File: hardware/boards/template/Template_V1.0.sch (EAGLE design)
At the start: 2 parts

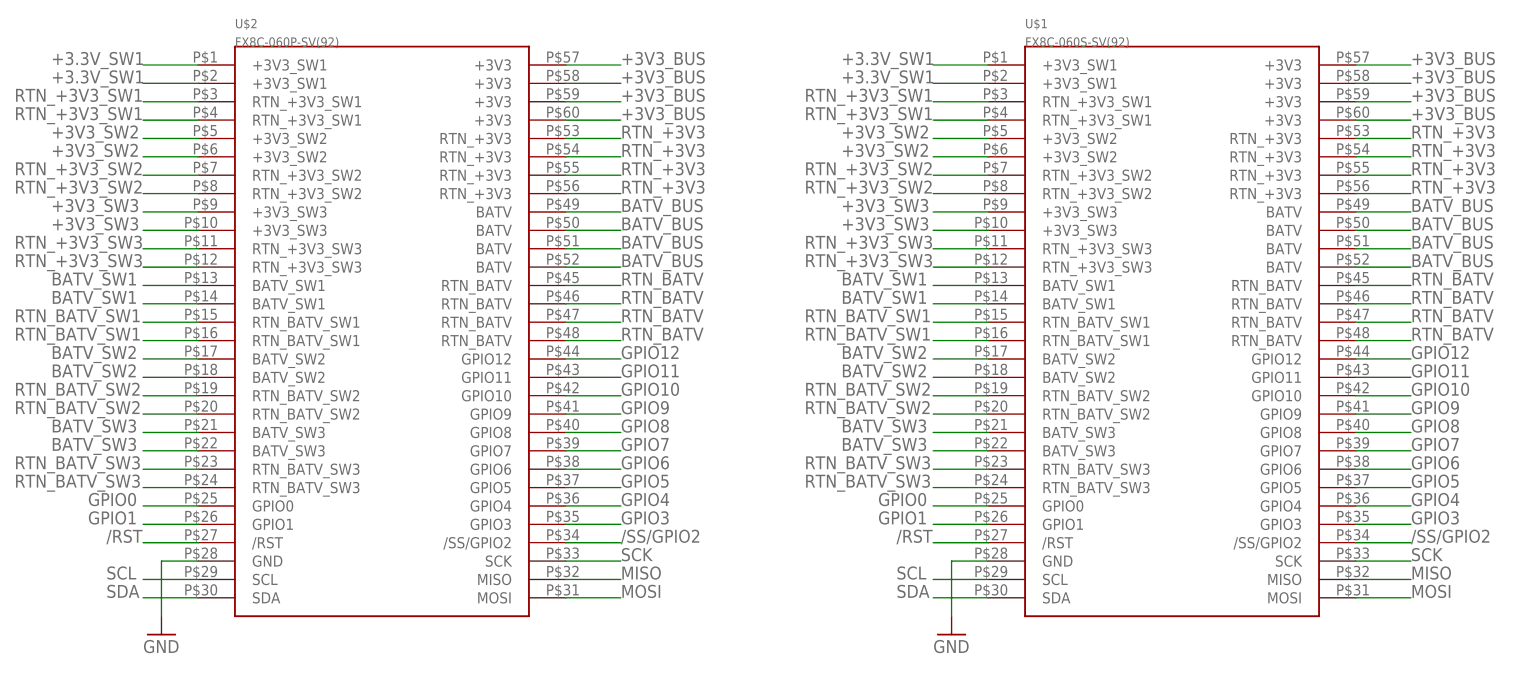
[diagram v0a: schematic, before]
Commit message: fixed fx8c symbols
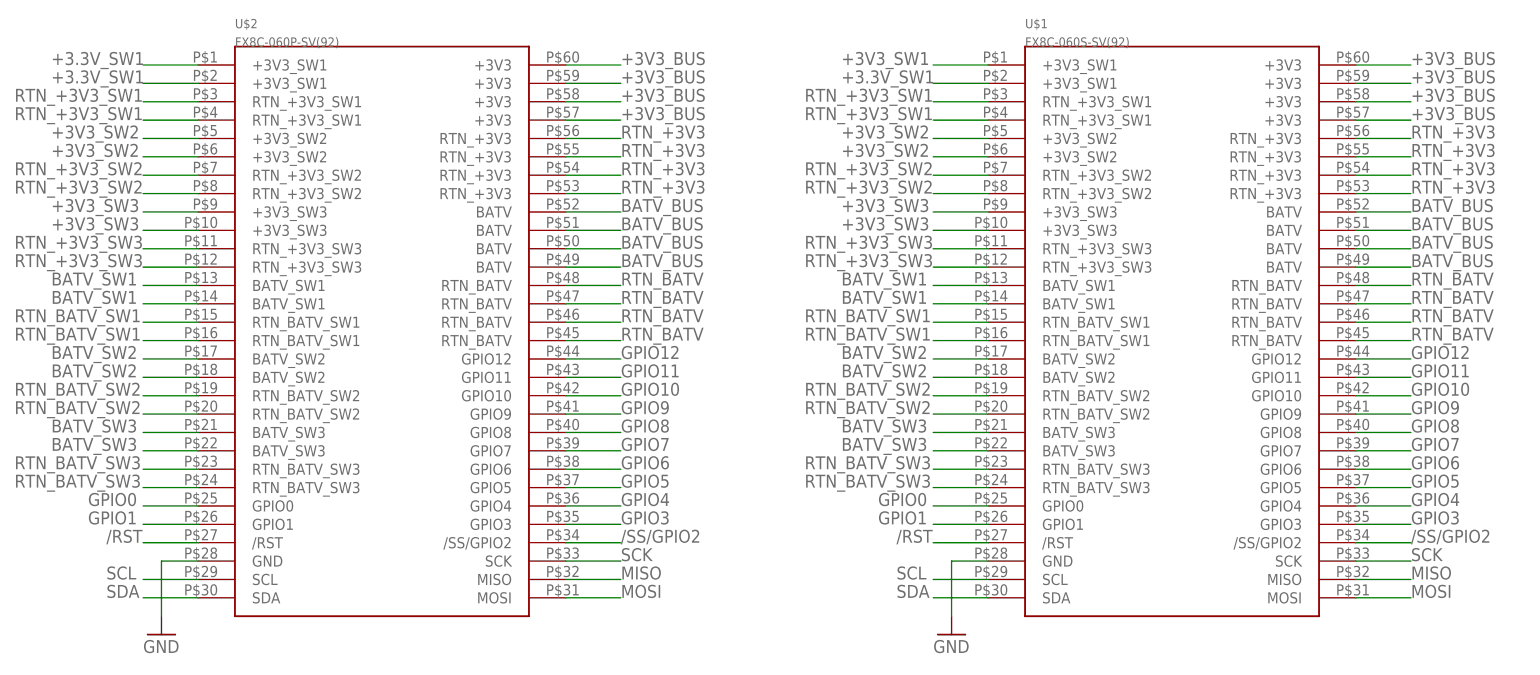
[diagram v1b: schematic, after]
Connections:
- new net +3V3_SW1: U$1.+3V3_SW1@1
- net +3.3V_SW1: no longer U$1.+3V3_SW1@1
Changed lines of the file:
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@@
 <grid distance="0.1" unitdist="inch" unit="inch" style="lines" multiple="1" display="no" altdistance="0.01" altunitdist="inch" altunit="inch"/>
 <layers>
-<layer number="1" name="Top" color="4" fill="1" visible="no" active="no"/>
-<layer number="16" name="Bottom" color="1" fill="1" visible="no" active="no"/>
-<layer number="17" name="Pads" color="2" fill="1" visible="no" active="no"/>
-<layer number="18" name="Vias" color="2" fill="1" visible="no" active="no"/>
-<layer number="19" name="Unrouted" color="6" fill="1" visible="no" active="no"/>
-<layer number="20" name="Dimension" color="15" fill="1" visible="no" active="no"/>
-<layer number="21" name="tPlace" color="7" fill="1" visible="no" active="no"/>
-<layer number="22" name="bPlace" color="7" fill="1" visible="no" active="no"/>
-<layer number="23" name="tOrigins" color="15" fill="1" visible="no" active="no"/>
-<layer number="24" name="bOrigins" color="15" fill="1" visible="no" active="no"/>
-<layer number="25" name="tNames" color="7" fill="1" visible="no" active="no"/>
-<layer number="26" name="bNames" color="7" fill="1" visible="no" active="no"/>
-<layer number="27" name="tValues" color="7" fill="1" visible="no" active="no"/>
-<layer number="28" name="bValues" color="7" fill="1" visible="no" active="no"/>
+<layer number="1" name="Top" color="4" fill="1" visible="yes" active="no"/>
+<layer number="16" name="Bottom" color="1" fill="1" visible="yes" active="no"/>
+<layer number="17" name="Pads" color="2" fill="1" visible="yes" active="no"/>
+<layer number="18" name="Vias" color="2" fill="1" visible="yes" active="no"/>
+<layer number="19" name="Unrouted" color="6" fill="1" visible="yes" active="no"/>
+<layer number="20" name="Dimension" color="15" fill="1" visible="yes" active="no"/>
+<layer number="21" name="tPlace" color="7" fill="1" visible="yes" active="no"/>
+<layer number="22" name="bPlace" color="7" fill="1" visible="yes" active="no"/>
+<layer number="23" name="tOrigins" color="15" fill="1" visible="yes" active="no"/>
+<layer number="24" name="bOrigins" color="15" fill="1" visible="yes" active="no"/>
+<layer number="25" name="tNames" color="7" fill="1" visible="yes" active="no"/>
+<layer number="26" name="bNames" color="7" fill="1" visible="yes" active="no"/>
+<layer number="27" name="tValues" color="7" fill="1" visible="yes" active="no"/>
+<layer number="28" name="bValues" color="7" fill="1" visible="yes" active="no"/>
 <layer number="29" name="tStop" color="7" fill="3" visible="no" active="no"/>
 <layer number="30" name="bStop" color="7" fill="6" visible="no" active="no"/>
@@
 <layer number="35" name="tGlue" color="7" fill="4" visible="no" active="no"/>
 <layer number="36" name="bGlue" color="7" fill="5" visible="no" active="no"/>
-<layer number="37" name="tTest" color="7" fill="1" visible="no" active="no"/>
-<layer number="38" name="bTest" color="7" fill="1" visible="no" active="no"/>
+<layer number="37" name="tTest" color="7" fill="1" visible="yes" active="no"/>
+<layer number="38" name="bTest" color="7" fill="1" visible="yes" active="no"/>
 <layer number="39" name="tKeepout" color="4" fill="11" visible="no" active="no"/>
 <layer number="40" name="bKeepout" color="1" fill="11" visible="no" active="no"/>
@@
 <layer number="44" name="Drills" color="7" fill="1" visible="no" active="no"/>
 <layer number="45" name="Holes" color="7" fill="1" visible="no" active="no"/>
-<layer number="46" name="Milling" color="3" fill="1" visible="no" active="no"/>
-<layer number="47" name="Measures" color="7" fill="1" visible="no" active="no"/>
-<layer number="48" name="Document" color="7" fill="1" visible="no" active="no"/>
-<layer number="49" name="Reference" color="7" fill="1" visible="no" active="no"/>
-<layer number="50" name="dxf" color="7" fill="1" visible="no" active="no"/>
-<layer number="51" name="tDocu" color="7" fill="1" visible="no" active="no"/>
-<layer number="52" name="bDocu" color="7" fill="1" visible="no" active="no"/>
-<layer number="53" name="tGND_GNDA" color="7" fill="9" visible="no" active="no"/>
-<layer number="54" name="bGND_GNDA" color="1" fill="9" visible="no" active="no"/>
-<layer number="56" name="wert" color="7" fill="1" visible="no" active="no"/>
-<layer number="57" name="tCAD" color="7" fill="1" visible="no" active="no"/>
+<layer number="46" name="Milling" color="3" fill="1" visible="yes" active="no"/>
+<layer number="47" name="Measures" color="7" fill="1" visible="yes" active="no"/>
+<layer number="48" name="Document" color="7" fill="1" visible="yes" active="no"/>
+<layer number="49" name="Reference" color="7" fill="1" visible="yes" active="no"/>
+<layer number="50" name="dxf" color="7" fill="1" visible="yes" active="no"/>
+<layer number="51" name="tDocu" color="7" fill="1" visible="yes" active="no"/>
+<layer number="52" name="bDocu" color="7" fill="1" visible="yes" active="no"/>
+<layer number="53" name="tGND_GNDA" color="7" fill="9" visible="yes" active="no"/>
+<layer number="54" name="bGND_GNDA" color="1" fill="9" visible="yes" active="no"/>
+<layer number="56" name="wert" color="7" fill="1" visible="yes" active="no"/>
+<layer number="57" name="tCAD" color="7" fill="1" visible="yes" active="no"/>
 <layer number="90" name="Modules" color="5" fill="1" visible="yes" active="yes"/>
 <layer number="91" name="Nets" color="2" fill="1" visible="yes" active="yes"/>
@@
 </segment>
 <segment>
-<wire x1="170.18" y1="137.16" x2="162.56" y2="137.16" width="0.1524" layer="91"/>
-<label x="149.86" y="137.16" size="1.778" layer="95"/>
-<pinref part="U$1" gate="G$1" pin="+3V3_SW1@1"/>
-</segment>
-<segment>
 <wire x1="170.18" y1="134.62" x2="162.56" y2="134.62" width="0.1524" layer="91"/>
 <label x="149.86" y="134.62" size="1.778" layer="95"/>
@@
 </segment>
 </net>
+<net name="+3V3_SW1" class="0">
+<segment>
+<wire x1="170.18" y1="137.16" x2="162.56" y2="137.16" width="0.1524" layer="91"/>
+<label x="149.86" y="137.16" size="1.778" layer="95"/>
+<pinref part="U$1" gate="G$1" pin="+3V3_SW1@1"/>
+</segment>
+</net>
